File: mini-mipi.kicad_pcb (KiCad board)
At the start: 4 copper layers, 43.2 x 34.9 mm, 69 parts, among them IC1 ECP5-BGA256, J1 Conn_ARM_JTAG_SWD_10, J2 Conn_01x15, J3 USB_B_Micro, J4 Micro_SD_Card, U1 AP3429-A, U2 TPS74625, U3 AP3429-A, U4 TPS74611, U5 AT25SF081-SSHD-X, U6 S27KL0641, U7 SI5351A-B-GTR, Y1 Crystal_GND24

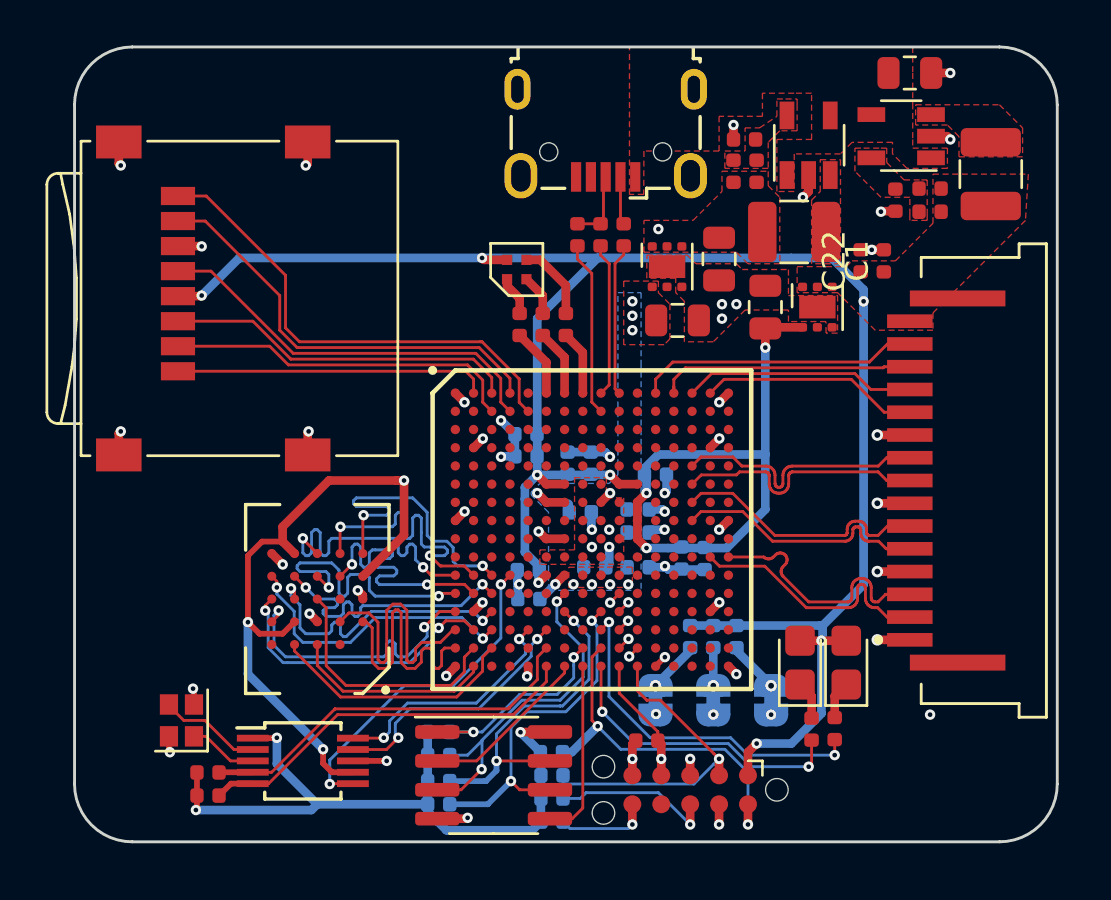
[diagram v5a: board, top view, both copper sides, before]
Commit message: Change debug header to 2.54mm standard
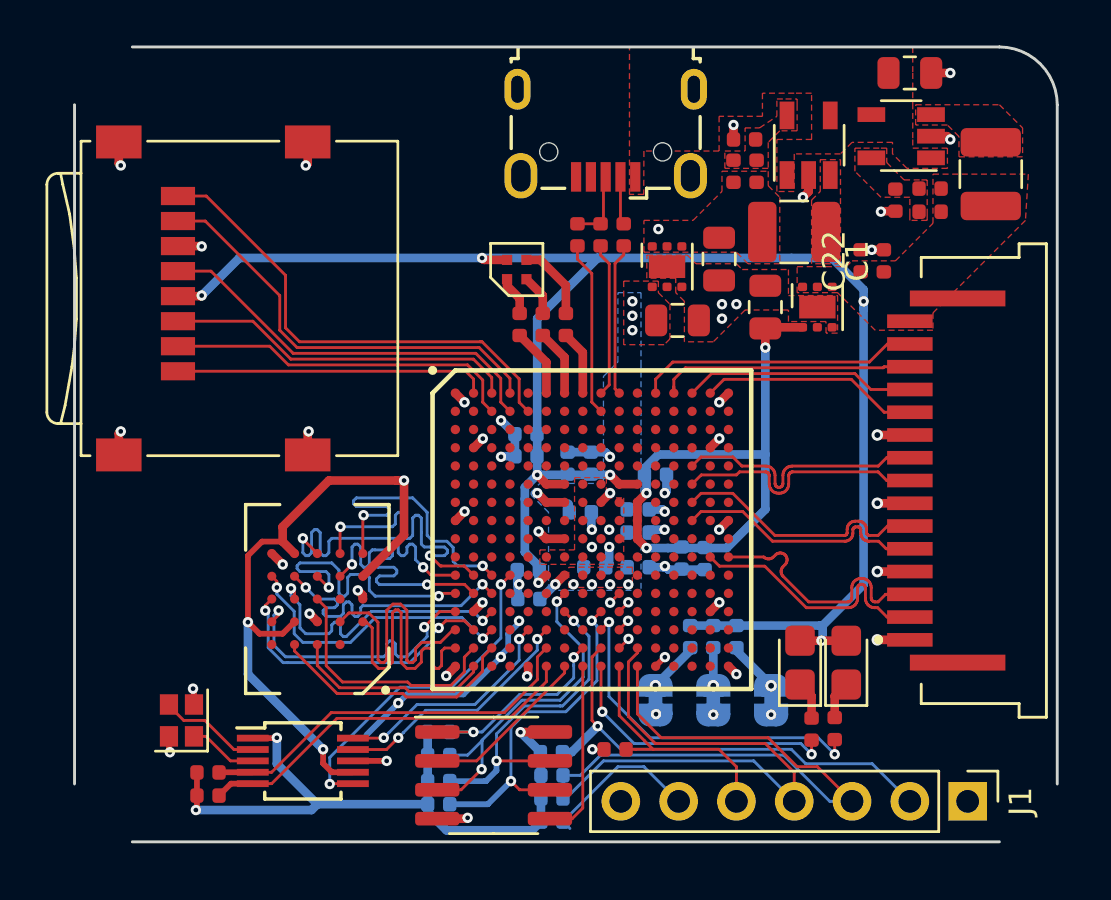
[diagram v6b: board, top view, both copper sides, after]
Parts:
- J1: value Conn_ARM_JTAG_SWD_10 -> Conn_01x07; footprint Connector:Tag-Connect_TC2050-IDC-NL_2x05_P1.27mm_Vertical -> Connector_PinHeader_2.54mm:PinHeader_1x07_P2.54mm_Vertical
- moved J1 12.2 mm to (180.8, 95.4), turned to -90 degrees
- moved R20 1.45 mm to (165.4, 93.1)
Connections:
- J1 pad 1: VCC -> GND
- J1 pad 2: /CONFIG/TMS -> /CONFIG/~RESET
- J1 pad 3: GND -> /CONFIG/TMS
- J1 pad 4: /CONFIG/TCK -> /CONFIG/TDI
- J1 pad 5: GND -> /CONFIG/TCK
- J1 pad 7: Net-(J1-Pad7) -> VCC
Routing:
- net /CONFIG/TMS: track 14.3 -> 27.4 mm, vias 1 -> 0
- net /CONFIG/TDI: track 16.2 -> 24.3 mm, vias 2 -> 0
- net GND: track 44.2 -> 50.3 mm, vias 55 -> 56
- net /CONFIG/TCK: track 5.56 -> 11.0 mm, vias 1 -> 0
- net /CONFIG/~RESET: track 16.6 -> 21.1 mm, vias 2 -> 1
- net VCC: track 125.8 -> 123.2 mm, vias 12 -> 10
- net /CONFIG/TDO: track 15.2 -> 17.7 mm, vias 2 -> 1
- net Net-(IC1-PadT9): track 13.3 -> 12.6 mm
- net Net-(IC1-PadP6): track 11.5 -> 11.0 mm
- net Net-(IC1-PadP5): track 10.7 -> 10.2 mm

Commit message: Remove SD card, relocate regulators
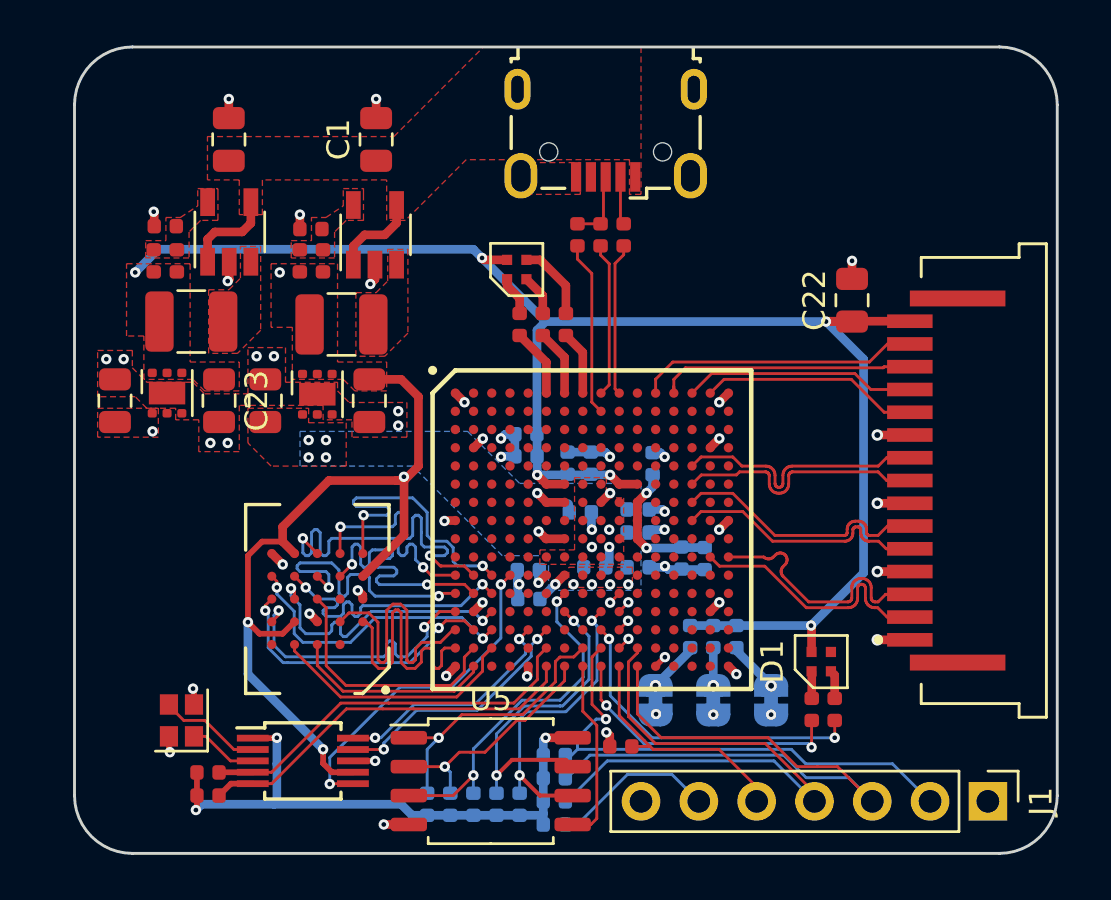
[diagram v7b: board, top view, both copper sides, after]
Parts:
- removed D2: LED, LED_SMD:LED_0805_2012Metric_Castellated
- removed J4: Micro_SD_Card, Connector_Card:microSD_HC_Wuerth_693072010801
- added C23: C, Capacitor_SMD:C_0805_2012Metric, F.Cu at (148.0, 77.8)
- added R25: 4.7k, Resistor_SMD:R_0402_1005Metric, B.Cu at (160.1, 95.5)
- C1, C22: footprint Capacitor_SMD:C_0402_1005Metric -> Capacitor_SMD:C_0805_2012Metric
- D1: value LED -> LED_RGBA; footprint LED_SMD:LED_0805_2012Metric_Castellated -> mini-mipi:LED_0404
- U5: footprint Package_SO:SOIC-8_3.9x4.9mm_P1.27mm -> Package_SO:SOIC-8_5.275x5.275mm_P1.27mm
- moved L1 35.7 mm to (146.7, 74.3), turned to 180 degrees
- moved C4 34.2 mm to (145.1, 71.6), turned to 90 degrees
- moved R23 33.2 mm to (146.1, 71.6), turned to 90 degrees
- moved R24 32.1 mm to (145.6, 70.1), turned to 180 degrees
- moved C3 30.1 mm to (148.4, 66.3), turned to 90 degrees
- moved U1 29.8 mm to (148.4, 70.4), turned to 90 degrees
- moved C7 28.9 mm to (143.4, 77.8)
- moved U2 28.8 mm to (145.7, 77.4)
- moved C1 22.9 mm to (154.9, 66.3)
- moved L3 20.3 mm to (153.3, 74.4)
- moved R27 19.5 mm to (152.5, 71.6)
- moved U3 19.5 mm to (154.8, 70.5)
- moved C21 19.5 mm to (151.5, 71.6)
- moved R28 19.5 mm to (152.0, 70.2)
- moved C8 18.5 mm to (150.0, 77.8), turned to 90 degrees
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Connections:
- C1 pad 1: VCC -> VBUS
- D1 pad 2: VCC -> Net-(D1-Pad2)
- IC1 pad A2: /SD_CARD/DAT2 -> Net-(IC1-PadA2)
- IC1 pad A3: /SD_CARD/CMD -> Net-(IC1-PadA3)
- IC1 pad A4: /SD_CARD/DAT0 -> Net-(IC1-PadA4)
- IC1 pad B3: /SD_CARD/DAT3 -> Net-(IC1-PadB3)
- IC1 pad B4: /SD_CARD/CLK -> Net-(IC1-PadB4)
- IC1 pad B5: /SD_CARD/DAT1 -> Net-(IC1-PadB5)
- R18 pad 2: /CONFIG/DIO2 -> /CONFIG/DIO1
- R19 pad 1: /CONFIG/DIO3 -> /CONFIG/DIO2
- R5 pad 2: Net-(D2-Pad1) -> Net-(D1-Pad2)
- U2 pad 4: Net-(U2-Pad4) -> VCC
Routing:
- net /SD_CARD/DAT1: track 21.3 -> 0.00 mm
- net /SD_CARD/DAT0: track 19.0 -> 0.00 mm
- net /SD_CARD/CLK: track 17.8 -> 0.00 mm
- net VCC: track 123.2 -> 140.0 mm
- net /SD_CARD/DAT3: track 15.5 -> 0.00 mm
- net /SD_CARD/CMD: track 15.5 -> 0.00 mm
- net GND: track 50.3 -> 35.6 mm, vias 56 -> 54
- net /SD_CARD/DAT2: track 13.7 -> 0.00 mm
- net +1V8: track 55.1 -> 43.4 mm
- net VBUS: track 0.00 -> 8.04 mm
- net /CONFIG/CSN: track 9.50 -> 12.4 mm, vias 2 -> 1
- net /CONFIG/DIO1: track 7.49 -> 10.3 mm, vias 0 -> 1
- net +2V5: track 31.2 -> 33.3 mm
- net /CONFIG/TMS: track 27.4 -> 29.5 mm
- net /CONFIG/MCK: track 15.3 -> 13.4 mm
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- added copper zone on F.Cu, net +2V5
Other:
- board size 43.2 x 34.9 mm -> 43.2 x 35.4 mm

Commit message: Fix incorrect flash CSN pin
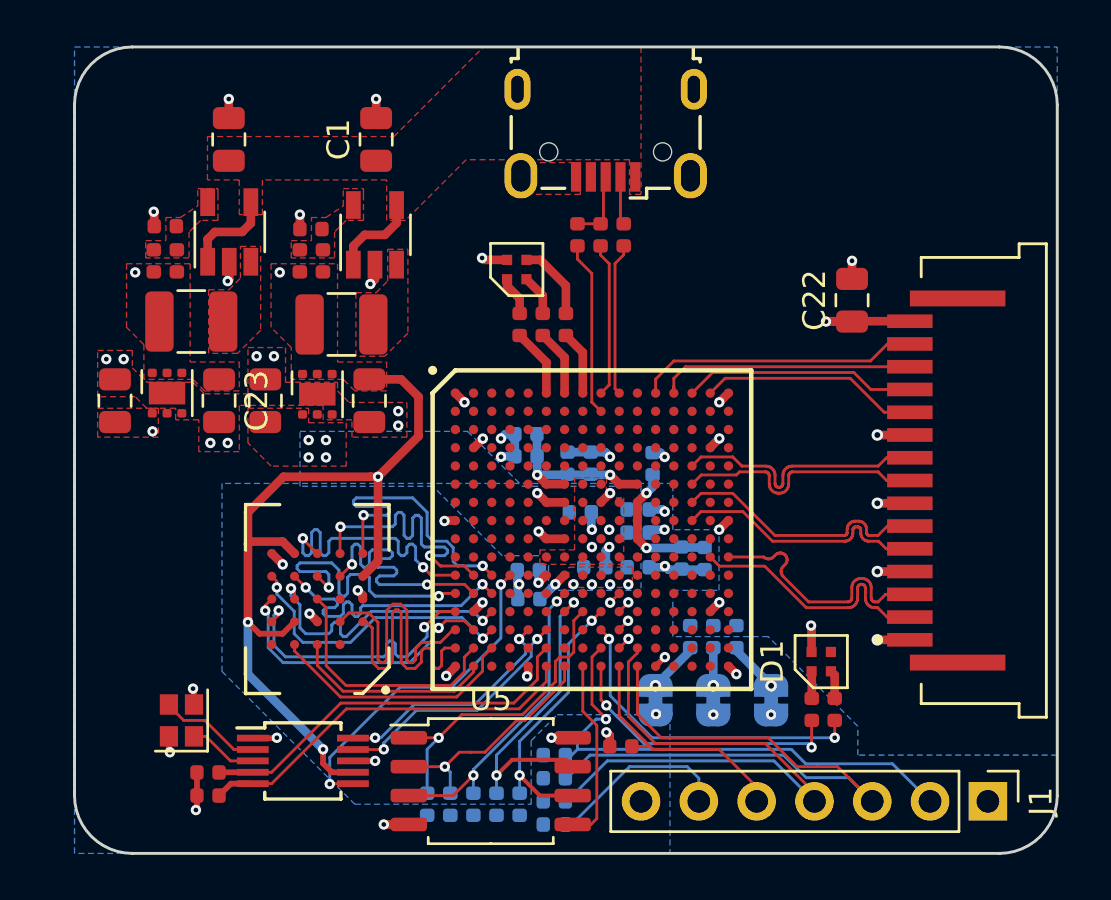
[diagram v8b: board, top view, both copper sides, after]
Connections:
- IC1 pad N8: Net-(IC1-PadN8) -> /CONFIG/CSN
- IC1 pad R8: /CONFIG/CSN -> Net-(IC1-PadR8)
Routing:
- net VCC: track 140.0 -> 59.6 mm
- net +1V8: track 43.4 -> 45.7 mm
- net /CONFIG/DIO2: track 15.6 -> 13.6 mm
- net /CONFIG/CSN: track 12.4 -> 13.9 mm
- net /CONFIG/MCK: track 13.4 -> 12.2 mm
- net /CONFIG/DIO3: track 14.8 -> 14.1 mm
- added copper zone on B.Cu, net VCC
